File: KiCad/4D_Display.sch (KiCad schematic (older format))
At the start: 10 parts

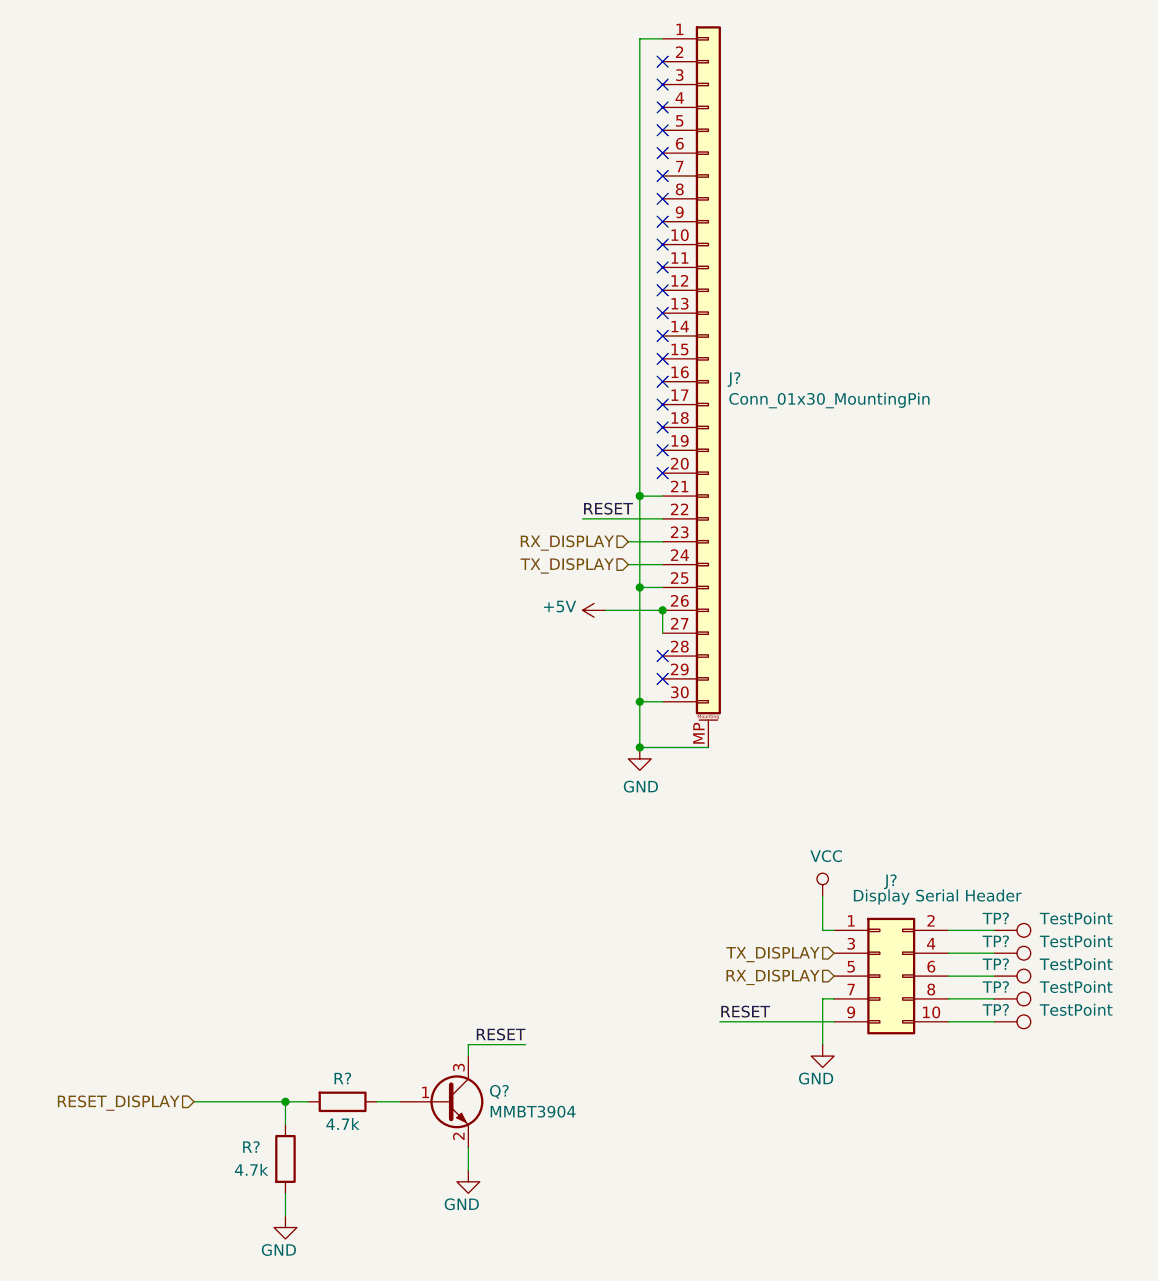
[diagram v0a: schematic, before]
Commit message: Fixing ERC rules
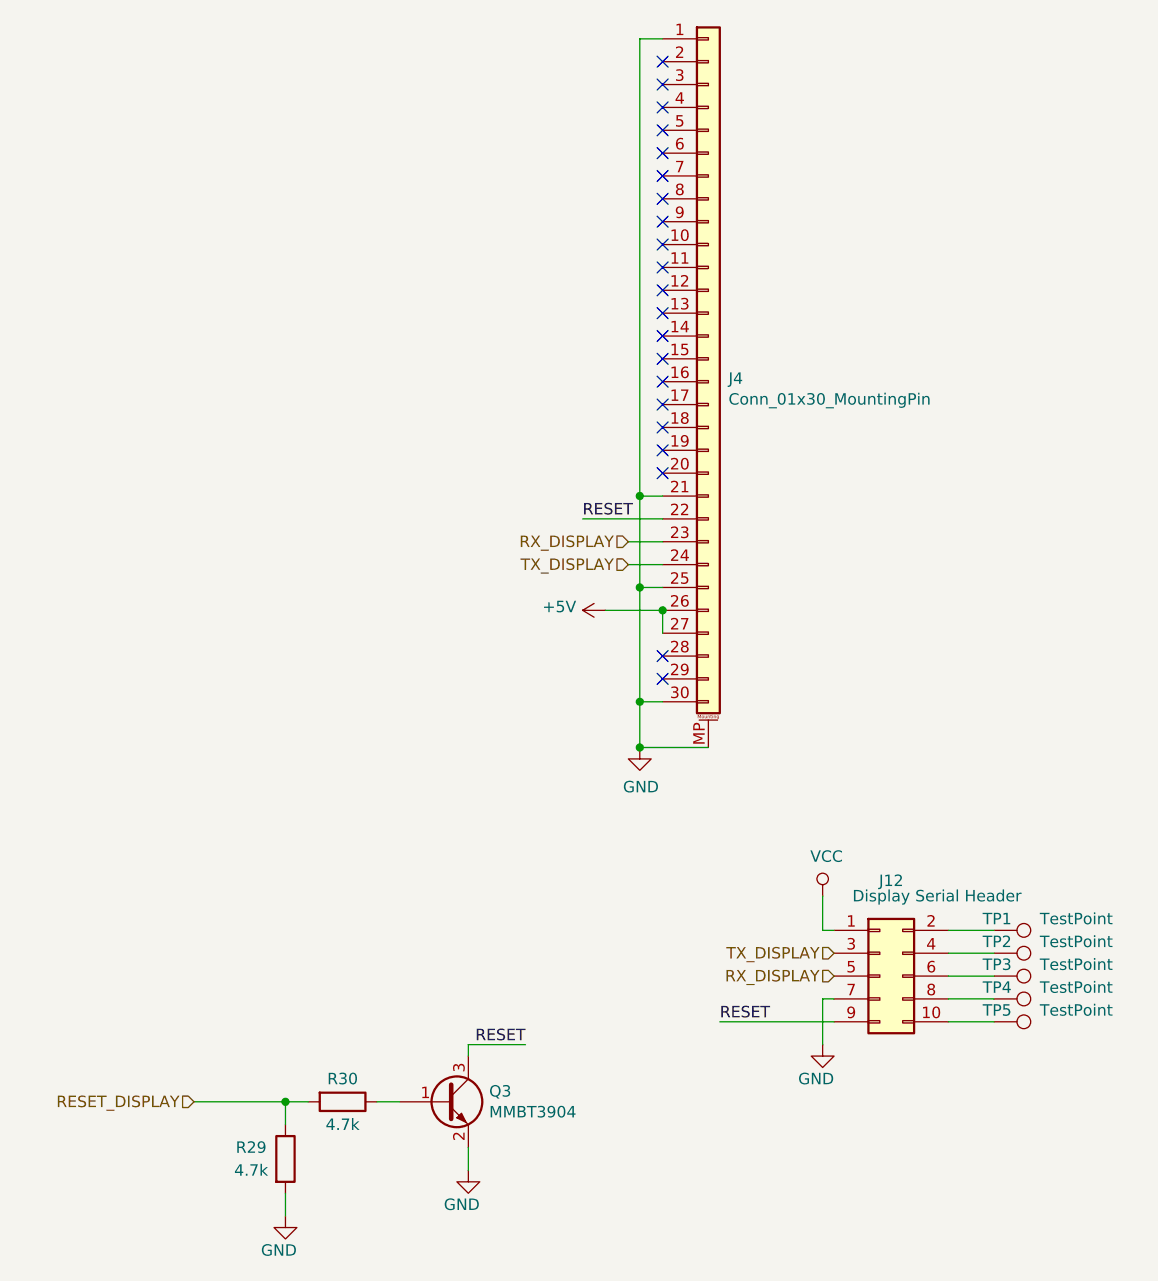
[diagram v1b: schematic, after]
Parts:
- gave numbers to parts that had none: 10
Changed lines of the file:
@@
 	5100 5500 5100 5350
 $Comp
-L power:VCC #PWR?
+L power:VCC #PWR0151
 U 1 1 5DD6C26E
 P 5100 5350
-F 0 "#PWR?" H 5100 5200 50  0001 C CNN
+F 0 "#PWR0151" H 5100 5200 50  0001 C CNN
 F 1 "VCC" H 5117 5523 50  0000 C CNN
 F 2 "" H 5100 5350 50  0001 C CNN
@@
 AR Path="/5BCD883C/5DD6C276" Ref="TP?"  Part="1"
 AR Path="/5DD6C276" Ref="TP?"  Part="1"
-AR Path="/5DD3CEE8/5DD6C276" Ref="TP?"  Part="1"
-F 0 "TP?" V 5800 5450 50  0000 L CNN
+AR Path="/5DD3CEE8/5DD6C276" Ref="TP1"  Part="1"
+F 0 "TP1" V 5800 5450 50  0000 L CNN
 F 1 "TestPoint" V 5800 5700 50  0000 L CNN
 F 2 "Snack Machine:TestPoint_THTPad_D0.8mm_Drill0.4mm" H 6050 5500 50  0001 C CNN
@@
 AR Path="/5BCD883C/5DD6C27D" Ref="TP?"  Part="1"
 AR Path="/5DD6C27D" Ref="TP?"  Part="1"
-AR Path="/5DD3CEE8/5DD6C27D" Ref="TP?"  Part="1"
-F 0 "TP?" V 5800 5550 50  0000 L CNN
+AR Path="/5DD3CEE8/5DD6C27D" Ref="TP2"  Part="1"
+F 0 "TP2" V 5800 5550 50  0000 L CNN
 F 1 "TestPoint" V 5800 5800 50  0000 L CNN
 F 2 "Snack Machine:TestPoint_THTPad_D0.8mm_Drill0.4mm" H 6050 5600 50  0001 C CNN
@@
 AR Path="/5BCD883C/5DD6C284" Ref="TP?"  Part="1"
 AR Path="/5DD6C284" Ref="TP?"  Part="1"
-AR Path="/5DD3CEE8/5DD6C284" Ref="TP?"  Part="1"
-F 0 "TP?" V 5800 5650 50  0000 L CNN
+AR Path="/5DD3CEE8/5DD6C284" Ref="TP3"  Part="1"
+F 0 "TP3" V 5800 5650 50  0000 L CNN
 F 1 "TestPoint" V 5800 5900 50  0000 L CNN
 F 2 "Snack Machine:TestPoint_THTPad_D0.8mm_Drill0.4mm" H 6050 5700 50  0001 C CNN
@@
 AR Path="/5BCD883C/5DD6C28B" Ref="TP?"  Part="1"
 AR Path="/5DD6C28B" Ref="TP?"  Part="1"
-AR Path="/5DD3CEE8/5DD6C28B" Ref="TP?"  Part="1"
-F 0 "TP?" V 5800 5750 50  0000 L CNN
+AR Path="/5DD3CEE8/5DD6C28B" Ref="TP4"  Part="1"
+F 0 "TP4" V 5800 5750 50  0000 L CNN
 F 1 "TestPoint" V 5800 6000 50  0000 L CNN
 F 2 "Snack Machine:TestPoint_THTPad_D0.8mm_Drill0.4mm" H 6050 5800 50  0001 C CNN
@@
 AR Path="/5BCD883C/5DD6C292" Ref="TP?"  Part="1"
 AR Path="/5DD6C292" Ref="TP?"  Part="1"
-AR Path="/5DD3CEE8/5DD6C292" Ref="TP?"  Part="1"
-F 0 "TP?" V 5800 5850 50  0000 L CNN
+AR Path="/5DD3CEE8/5DD6C292" Ref="TP5"  Part="1"
+F 0 "TP5" V 5800 5850 50  0000 L CNN
 F 1 "TestPoint" V 5800 6100 50  0000 L CNN
 F 2 "Snack Machine:TestPoint_THTPad_D0.8mm_Drill0.4mm" H 6050 5900 50  0001 C CNN
@@
 	5150 5800 5100 5800
 $Comp
-L power:GND #PWR?
+L power:GND #PWR0152
 U 1 1 5DD6C299
 P 5100 6000
-F 0 "#PWR?" H 5100 5750 50  0001 C CNN
+F 0 "#PWR0152" H 5100 5750 50  0001 C CNN
 F 1 "GND" H 5150 5850 50  0000 R CNN
 F 2 "" H 5100 6000 50  0001 C CNN
@@
 	5100 5800 5100 6000
 $Comp
-L Connector_Generic:Conn_02x05_Odd_Even J?
+L Connector_Generic:Conn_02x05_Odd_Even J12
 U 1 1 5DD6C2A3
 P 5350 5700
-F 0 "J?" H 5400 6117 50  0000 C CNN
+F 0 "J12" H 5400 6117 50  0000 C CNN
 F 1 "Display Serial Header" H 5600 6050 50  0000 C CNN
 F 2 "Connector_PinSocket_2.54mm:PinSocket_2x05_P2.54mm_Vertical" H 5350 5700 50  0001 C CNN
@@
 AR Path="/5BA75957/5DD6C2AB" Ref="Q?"  Part="1"
 AR Path="/5DD6C2AB" Ref="Q?"  Part="1"
-AR Path="/5DD3CEE8/5DD6C2AB" Ref="Q?"  Part="1"
-F 0 "Q?" H 3641 6296 50  0000 L CNN
+AR Path="/5DD3CEE8/5DD6C2AB" Ref="Q3"  Part="1"
+F 0 "Q3" H 3641 6296 50  0000 L CNN
 F 1 "MMBT3904" H 3641 6205 50  0000 L CNN
 F 2 "Snack Machine:SOT-23_Handsoldering_Lite" H 3650 6175 50  0001 L CIN
@@
 $EndComp
 $Comp
-L Device:R R?
+L Device:R R29
 U 1 1 5DD6C2B3
 P 2750 6500
-F 0 "R?" H 2600 6550 50  0000 C CNN
+F 0 "R29" H 2600 6550 50  0000 C CNN
 F 1 "4.7k" H 2600 6450 50  0000 C CNN
 F 2 "Resistor_SMD:R_0603_1608Metric_Pad1.05x0.95mm_HandSolder" V 2680 6500 50  0001 C CNN
@@
 $EndComp
 $Comp
-L Device:R R?
+L Device:R R30
 U 1 1 5DD6C2BB
 P 3000 6250
-F 0 "R?" V 2900 6250 50  0000 C CNN
+F 0 "R30" V 2900 6250 50  0000 C CNN
 F 1 "4.7k" V 3100 6250 50  0000 C CNN
 F 2 "Resistor_SMD:R_0603_1608Metric_Pad1.05x0.95mm_HandSolder" V 2930 6250 50  0001 C CNN
@@
 $EndComp
 $Comp
-L power:GND #PWR?
+L power:GND #PWR0153
 U 1 1 5DD6C2C1
 P 2750 6750
-F 0 "#PWR?" H 2750 6500 50  0001 C CNN
+F 0 "#PWR0153" H 2750 6500 50  0001 C CNN
 F 1 "GND" H 2800 6600 50  0000 R CNN
 F 2 "" H 2750 6750 50  0001 C CNN
@@
 $EndComp
 $Comp
-L power:GND #PWR?
+L power:GND #PWR0154
 U 1 1 5DD6C2C7
 P 3550 6550
-F 0 "#PWR?" H 3550 6300 50  0001 C CNN
+F 0 "#PWR0154" H 3550 6300 50  0001 C CNN
 F 1 "GND" H 3600 6400 50  0000 R CNN
 F 2 "" H 3550 6550 50  0001 C CNN
@@
 Connection ~ 2750 6250
 $Comp
-L Connector_Generic_MountingPin:Conn_01x30_MountingPin J?
+L Connector_Generic_MountingPin:Conn_01x30_MountingPin J4
 U 1 1 5DB44749
 P 4600 3000
-F 0 "J?" H 4688 2914 50  0000 L CNN
+F 0 "J4" H 4688 2914 50  0000 L CNN
 F 1 "Conn_01x30_MountingPin" H 4688 2823 50  0000 L CNN
 F 2 "" H 4600 3000 50  0001 C CNN
@@
 Connection ~ 4300 4500
 $Comp
-L power:GND #PWR?
+L power:GND #PWR0155
 U 1 1 5DB48D6A
 P 4300 4700
-F 0 "#PWR?" H 4300 4450 50  0001 C CNN
+F 0 "#PWR0155" H 4300 4450 50  0001 C CNN
 F 1 "GND" H 4305 4527 50  0000 C CNN
 F 2 "" H 4300 4700 50  0001 C CNN
@@
 Connection ~ 4400 4100
 $Comp
-L power:+5V #PWR?
+L power:+5V #PWR0156
 U 1 1 5DB4A1E4
 P 4150 4100
-F 0 "#PWR?" H 4150 3950 50  0001 C CNN
+F 0 "#PWR0156" H 4150 3950 50  0001 C CNN
 F 1 "+5V" V 4165 4228 50  0000 L CNN
 F 2 "" H 4150 4100 50  0001 C CNN

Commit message: Current WIP for board layout
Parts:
- removed TP1, TP2, TP3, TP4, TP5: TestPoint, Snack Machine:TestPoint_THTPad_D0.8mm_Drill0.4mm, symbol Connector:TestPoint
- J12: footprint Connector_PinSocket_2.54mm:PinSocket_2x05_P2.54mm_Vertical -> Snack Machine:PinHeader_2x05_P2.54mm_Vertical
- J4: value Conn_01x30_MountingPin -> V2 Display Ribbon Cable; footprint (none) -> Snack Machine:FPC30
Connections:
- net VCC is gone; now on net +5V: J12.1 (Pin_1)
- no-connect marks 21 -> 26
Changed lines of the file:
@@
 Wire Wire Line
 	5100 5500 5100 5350
-$Comp
-L power:VCC #PWR0151
-U 1 1 5DD6C26E
-P 5100 5350
-F 0 "#PWR0151" H 5100 5200 50  0001 C CNN
-F 1 "VCC" H 5117 5523 50  0000 C CNN
-F 2 "" H 5100 5350 50  0001 C CNN
-F 3 "" H 5100 5350 50  0001 C CNN
-	1    5100 5350
-	1    0    0    -1
-$EndComp
-Wire Wire Line
-	5850 5500 5650 5500
-$Comp
-L Connector:TestPoint TP?
-U 1 1 5DD6C276
-P 5850 5500
-AR Path="/5BCD883C/5DD6C276" Ref="TP?"  Part="1"
-AR Path="/5DD6C276" Ref="TP?"  Part="1"
-AR Path="/5DD3CEE8/5DD6C276" Ref="TP1"  Part="1"
-F 0 "TP1" V 5800 5450 50  0000 L CNN
-F 1 "TestPoint" V 5800 5700 50  0000 L CNN
-F 2 "Snack Machine:TestPoint_THTPad_D0.8mm_Drill0.4mm" H 6050 5500 50  0001 C CNN
-F 3 "~" H 6050 5500 50  0001 C CNN
-	1    5850 5500
-	0    1    1    0
-$EndComp
-Wire Wire Line
-	5850 5600 5650 5600
-$Comp
-L Connector:TestPoint TP?
-U 1 1 5DD6C27D
-P 5850 5600
-AR Path="/5BCD883C/5DD6C27D" Ref="TP?"  Part="1"
-AR Path="/5DD6C27D" Ref="TP?"  Part="1"
-AR Path="/5DD3CEE8/5DD6C27D" Ref="TP2"  Part="1"
-F 0 "TP2" V 5800 5550 50  0000 L CNN
-F 1 "TestPoint" V 5800 5800 50  0000 L CNN
-F 2 "Snack Machine:TestPoint_THTPad_D0.8mm_Drill0.4mm" H 6050 5600 50  0001 C CNN
-F 3 "~" H 6050 5600 50  0001 C CNN
-	1    5850 5600
-	0    1    1    0
-$EndComp
-Wire Wire Line
-	5850 5700 5650 5700
-$Comp
-L Connector:TestPoint TP?
-U 1 1 5DD6C284
-P 5850 5700
-AR Path="/5BCD883C/5DD6C284" Ref="TP?"  Part="1"
-AR Path="/5DD6C284" Ref="TP?"  Part="1"
-AR Path="/5DD3CEE8/5DD6C284" Ref="TP3"  Part="1"
-F 0 "TP3" V 5800 5650 50  0000 L CNN
-F 1 "TestPoint" V 5800 5900 50  0000 L CNN
-F 2 "Snack Machine:TestPoint_THTPad_D0.8mm_Drill0.4mm" H 6050 5700 50  0001 C CNN
-F 3 "~" H 6050 5700 50  0001 C CNN
-	1    5850 5700
-	0    1    1    0
-$EndComp
-Wire Wire Line
-	5850 5800 5650 5800
-$Comp
-L Connector:TestPoint TP?
-U 1 1 5DD6C28B
-P 5850 5800
-AR Path="/5BCD883C/5DD6C28B" Ref="TP?"  Part="1"
-AR Path="/5DD6C28B" Ref="TP?"  Part="1"
-AR Path="/5DD3CEE8/5DD6C28B" Ref="TP4"  Part="1"
-F 0 "TP4" V 5800 5750 50  0000 L CNN
-F 1 "TestPoint" V 5800 6000 50  0000 L CNN
-F 2 "Snack Machine:TestPoint_THTPad_D0.8mm_Drill0.4mm" H 6050 5800 50  0001 C CNN
-F 3 "~" H 6050 5800 50  0001 C CNN
-	1    5850 5800
-	0    1    1    0
-$EndComp
-Wire Wire Line
-	5850 5900 5650 5900
-$Comp
-L Connector:TestPoint TP?
-U 1 1 5DD6C292
-P 5850 5900
-AR Path="/5BCD883C/5DD6C292" Ref="TP?"  Part="1"
-AR Path="/5DD6C292" Ref="TP?"  Part="1"
-AR Path="/5DD3CEE8/5DD6C292" Ref="TP5"  Part="1"
-F 0 "TP5" V 5800 5850 50  0000 L CNN
-F 1 "TestPoint" V 5800 6100 50  0000 L CNN
-F 2 "Snack Machine:TestPoint_THTPad_D0.8mm_Drill0.4mm" H 6050 5900 50  0001 C CNN
-F 3 "~" H 6050 5900 50  0001 C CNN
-	1    5850 5900
-	0    1    1    0
-$EndComp
 Wire Wire Line
 	5150 5800 5100 5800
@@
 F 0 "J12" H 5400 6117 50  0000 C CNN
 F 1 "Display Serial Header" H 5600 6050 50  0000 C CNN
-F 2 "Connector_PinSocket_2.54mm:PinSocket_2x05_P2.54mm_Vertical" H 5350 5700 50  0001 C CNN
+F 2 "Snack Machine:PinHeader_2x05_P2.54mm_Vertical" H 5350 5700 50  0001 C CNN
 F 3 "~" H 5350 5700 50  0001 C CNN
 	1    5350 5700
@@
 P 4600 3000
 F 0 "J4" H 4688 2914 50  0000 L CNN
-F 1 "Conn_01x30_MountingPin" H 4688 2823 50  0000 L CNN
-F 2 "" H 4600 3000 50  0001 C CNN
+F 1 "V2 Display Ribbon Cable" H 4688 2823 50  0000 L CNN
+F 2 "Snack Machine:FPC30" H 4600 3000 50  0001 C CNN
 F 3 "~" H 4600 3000 50  0001 C CNN
 	1    4600 3000
@@
 	4400 4100 4150 4100
 Connection ~ 4400 4100
-$Comp
-L power:+5V #PWR0156
-U 1 1 5DB4A1E4
-P 4150 4100
-F 0 "#PWR0156" H 4150 3950 50  0001 C CNN
-F 1 "+5V" V 4165 4228 50  0000 L CNN
-F 2 "" H 4150 4100 50  0001 C CNN
-F 3 "" H 4150 4100 50  0001 C CNN
-	1    4150 4100
-	0    -1   -1   0
-$EndComp
 NoConn ~ 4400 3300
 NoConn ~ 4400 3200
@@
 Wire Wire Line
 	4250 3800 4400 3800
+NoConn ~ 5650 5500
+NoConn ~ 5650 5600
+NoConn ~ 5650 5700
+NoConn ~ 5650 5800
+NoConn ~ 5650 5900
+$Comp
+L power:+5V #PWR0151
+U 1 1 5E060D8D
+P 5100 5350
+F 0 "#PWR0151" H 5100 5200 50  0001 C CNN
+F 1 "+5V" H 5115 5523 50  0000 C CNN
+F 2 "" H 5100 5350 50  0001 C CNN
+F 3 "" H 5100 5350 50  0001 C CNN
+	1    5100 5350
+	1    0    0    -1
+$EndComp
+$Comp
+L power:+5V #PWR0156
+U 1 1 5E0610F1
+P 4150 4100
+F 0 "#PWR0156" H 4150 3950 50  0001 C CNN
+F 1 "+5V" V 4165 4228 50  0000 L CNN
+F 2 "" H 4150 4100 50  0001 C CNN
+F 3 "" H 4150 4100 50  0001 C CNN
+	1    4150 4100
+	0    -1   -1   0
+$EndComp
 $EndSCHEMATC

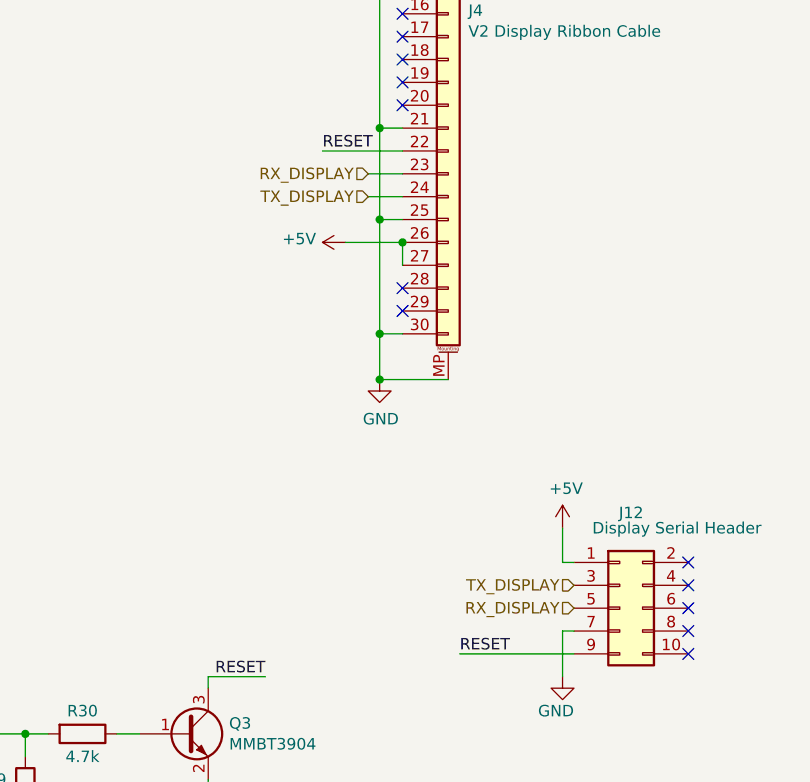
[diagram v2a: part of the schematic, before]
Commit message: Rotated serial ports around to make routing easier
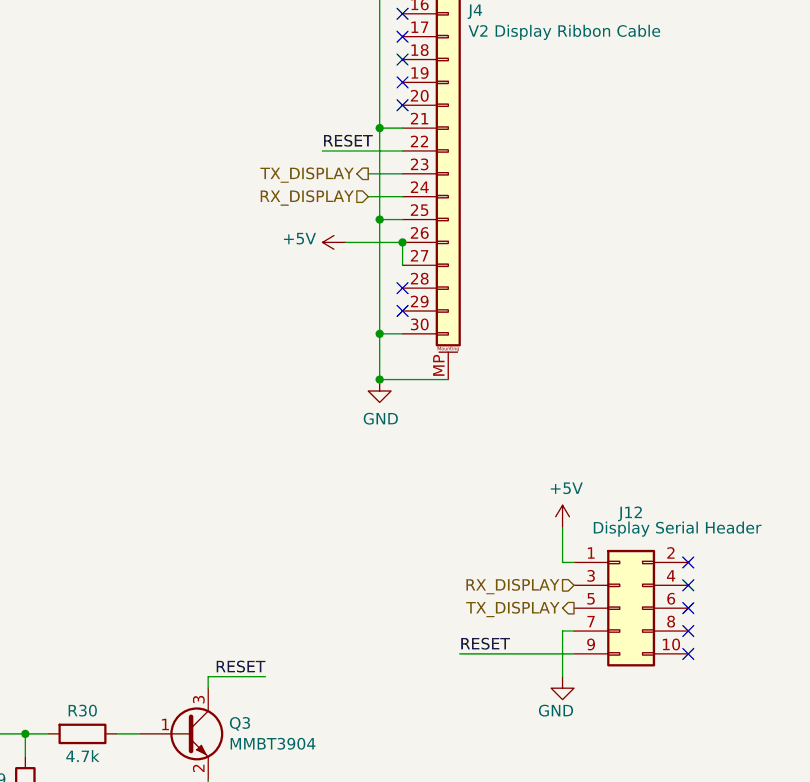
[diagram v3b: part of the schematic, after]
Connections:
- net RX_DISPLAY: now also J12.3 (Pin_3), J4.24 (Pin_24); no longer J12.5 (Pin_5), J4.23 (Pin_23)
- net TX_DISPLAY: now also J12.5 (Pin_5), J4.23 (Pin_23); no longer J12.3 (Pin_3), J4.24 (Pin_24)
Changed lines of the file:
@@
 	3550 6450 3550 6550
 Text HLabel 5150 5600 0    50   Input ~ 0
+RX_DISPLAY
+Text HLabel 5150 5700 0    50   Output ~ 0
 TX_DISPLAY
-Text HLabel 5150 5700 0    50   Input ~ 0
-RX_DISPLAY
 Text HLabel 2350 6250 0    50   Input ~ 0
 RESET_DISPLAY
@@
 Wire Wire Line
 	4050 3700 4400 3700
-Text HLabel 4250 3900 0    50   Input ~ 0
-TX_DISPLAY
 Wire Wire Line
 	4250 3900 4400 3900
-Text HLabel 4250 3800 0    50   Input ~ 0
-RX_DISPLAY
 Wire Wire Line
 	4250 3800 4400 3800
@@
 	0    -1   -1   0
 $EndComp
+Text HLabel 4250 3900 0    50   Input ~ 0
+RX_DISPLAY
+Text HLabel 4250 3800 0    50   Output ~ 0
+TX_DISPLAY
 $EndSCHEMATC

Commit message: Added part number, manufacturer, and personal bin numbers
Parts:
- J12: Manufacturer (none) -> TE Connectivity AMP Connectors; Part Number (none) -> 5103308-1
- J4: Manufacturer (none) -> TE Connectivity AMP Connectors; Part Number (none) -> 3-1734839-0
- Q3: Bin (none) -> 12
- R29, R30: Bin (none) -> 5
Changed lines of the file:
@@
 F 2 "Snack Machine:PinHeader_2x05_P2.54mm_Vertical" H 5350 5700 50  0001 C CNN
 F 3 "~" H 5350 5700 50  0001 C CNN
+F 4 "5103308-1" H 5350 5700 50  0001 C CNN "Part Number"
+F 5 "TE Connectivity AMP Connectors" H 5350 5700 50  0001 C CNN "Manufacturer"
 	1    5350 5700
 	1    0    0    -1
@@
 F 2 "Snack Machine:SOT-23_Handsoldering_Lite" H 3650 6175 50  0001 L CIN
 F 3 "https://www.fairchildsemi.com/datasheets/2N/2N3904.pdf" H 3450 6250 50  0001 L CNN
-F 4 "MMBT3904-TP" H 3450 6250 50  0001 C CNN "Part Number"
-F 5 "MCC" H 3450 6250 50  0001 C CNN "Manufacturer"
+F 4 "MCC" H 3450 6250 50  0001 C CNN "Manufacturer"
+F 5 "MMBT3904-TP" H 3450 6250 50  0001 C CNN "Part Number"
+F 6 "12" H 3450 6250 50  0001 C CNN "Bin"
 	1    3450 6250
 	1    0    0    -1
@@
 F 4 "RC0603FR-074K7L" H 2750 6500 50  0001 C CNN "Part Number"
 F 5 "Yageo" H 2750 6500 50  0001 C CNN "Manufacturer"
+F 6 "5" H 2750 6500 50  0001 C CNN "Bin"
 	1    2750 6500
 	1    0    0    -1
@@
 F 4 "RC0603FR-074K7L" V 3000 6250 50  0001 C CNN "Part Number"
 F 5 "Yageo" V 3000 6250 50  0001 C CNN "Manufacturer"
+F 6 "5" V 3000 6250 50  0001 C CNN "Bin"
 	1    3000 6250
 	0    1    1    0
@@
 F 2 "Snack Machine:FPC30" H 4600 3000 50  0001 C CNN
 F 3 "~" H 4600 3000 50  0001 C CNN
+F 4 "3-1734839-0" H 4600 3000 50  0001 C CNN "Part Number"
+F 5 "TE Connectivity AMP Connectors" H 4600 3000 50  0001 C CNN "Manufacturer"
 	1    4600 3000
 	1    0    0    -1
